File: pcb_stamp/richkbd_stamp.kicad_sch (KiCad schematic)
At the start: 52 parts, among them J1 USB_C_Receptacle_USB2.0, J2 OLED, K0 key-diode-led, K1 key-diode-led, K10 key-diode-led, K100 key-diode-led, K101 key-diode-led, K102 key-diode-led, K11 key-diode-led, K110 key-diode-led, K111 key-diode-led, K112 key-diode-led, K12 key-diode-led, K2 key-diode-led, K20 key-diode-led, K21 key-diode-led, K22 key-diode-led, K30 key-diode-led, K31 key-diode-led, K32 key-diode-led, K33 key-diode-led, K40 key-diode-led, K41 key-diode-led, K42 key-diode-led, K43 key-diode-led, K50 key-diode-led, K51 key-diode-led, K52 key-diode-led, K53 key-diode-led, K60 key-diode-led, K61 key-diode-led, K62 key-diode-led, K63 key-diode-led, K70 key-diode-led, K71 key-diode-led, K72 key-diode-led, K73 key-diode-led, K80 key-diode-led, K81 key-diode-led, K82 key-diode-led, K83 key-diode-led, K90 key-diode-led, K91 key-diode-led, K92 key-diode-led, U1 RP2040_Stamp

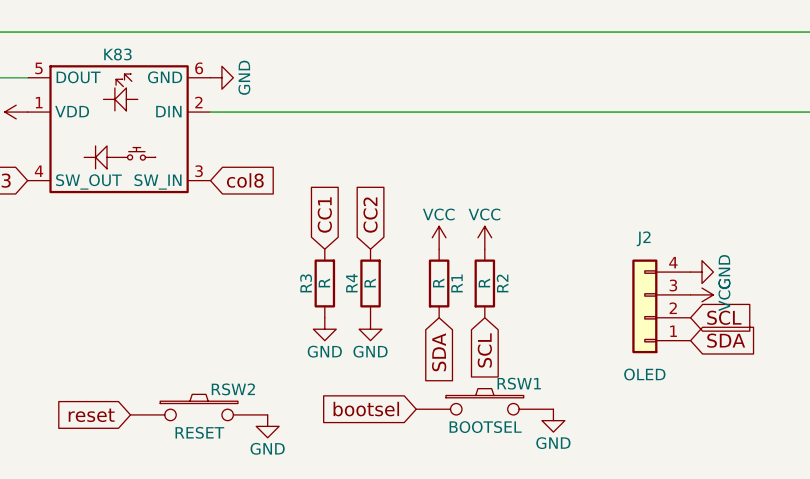
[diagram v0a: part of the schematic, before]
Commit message: Updated resistor values and moved lightsabres
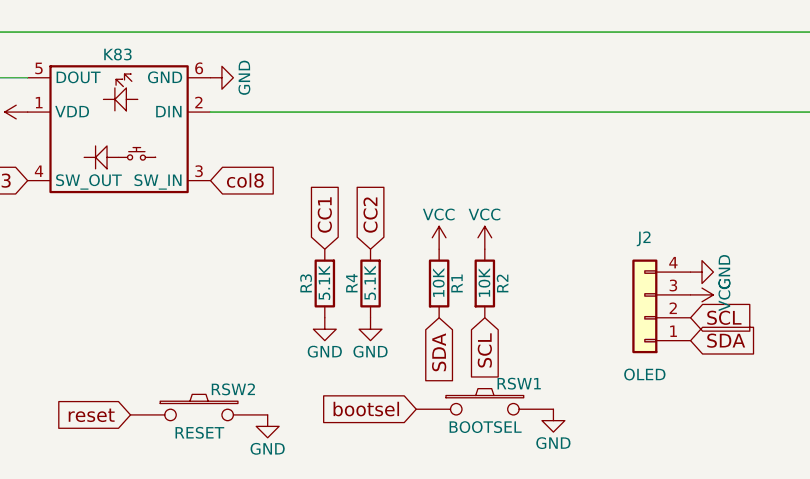
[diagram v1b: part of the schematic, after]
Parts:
- R1, R2: value R -> 10K
- R3, R4: value R -> 5.1K
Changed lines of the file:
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@@
     (in_bom yes) (on_board yes)
     (property "Reference" "R1" (id 0) (at 140.462 177.8 90))
-    (property "Value" "R" (id 1) (at 138.43 177.8 90))
+    (property "Value" "10K" (id 1) (at 138.43 177.8 90))
     (property "Footprint" "Resistor_SMD:R_0805_2012Metric" (id 2) (at 136.652 177.8 90)
       (effects (font (size 1.27 1.27)) hide)
@@
     (in_bom yes) (on_board yes)
     (property "Reference" "R2" (id 0) (at 145.542 177.8 90))
-    (property "Value" "R" (id 1) (at 143.51 177.8 90))
+    (property "Value" "10K" (id 1) (at 143.51 177.8 90))
     (property "Footprint" "Resistor_SMD:R_0805_2012Metric" (id 2) (at 141.732 177.8 90)
       (effects (font (size 1.27 1.27)) hide)
@@
     (in_bom yes) (on_board yes)
     (property "Reference" "R4" (id 0) (at 128.778 177.8 90))
-    (property "Value" "R" (id 1) (at 130.81 177.8 90))
+    (property "Value" "5.1K" (id 1) (at 130.81 177.8 90))
     (property "Footprint" "Resistor_SMD:R_0805_2012Metric" (id 2) (at 132.588 177.8 90)
       (effects (font (size 1.27 1.27)) hide)
@@
     (in_bom yes) (on_board yes)
     (property "Reference" "R3" (id 0) (at 123.698 177.8 90))
-    (property "Value" "R" (id 1) (at 125.73 177.8 90))
+    (property "Value" "5.1K" (id 1) (at 125.73 177.8 90))
     (property "Footprint" "Resistor_SMD:R_0805_2012Metric" (id 2) (at 127.508 177.8 90)
       (effects (font (size 1.27 1.27)) hide)
@@
     )
     (path "/00000000-0000-0000-0000-00005aa6d1f3"
-      (reference "R1") (unit 1) (value "R") (footprint "Resistor_SMD:R_0805_2012Metric")
+      (reference "R1") (unit 1) (value "10K") (footprint "Resistor_SMD:R_0805_2012Metric")
     )
     (path "/00000000-0000-0000-0000-00005aa6d2a6"
-      (reference "R2") (unit 1) (value "R") (footprint "Resistor_SMD:R_0805_2012Metric")
+      (reference "R2") (unit 1) (value "10K") (footprint "Resistor_SMD:R_0805_2012Metric")
     )
     (path "/dc4b8a19-92e0-4c35-a940-e928d580ba5b"
-      (reference "R3") (unit 1) (value "R") (footprint "Resistor_SMD:R_0805_2012Metric")
+      (reference "R3") (unit 1) (value "5.1K") (footprint "Resistor_SMD:R_0805_2012Metric")
     )
     (path "/387971ed-abb9-4f95-a329-18b3cdb7e9ad"
-      (reference "R4") (unit 1) (value "R") (footprint "Resistor_SMD:R_0805_2012Metric")
+      (reference "R4") (unit 1) (value "5.1K") (footprint "Resistor_SMD:R_0805_2012Metric")
     )
     (path "/00000000-0000-0000-0000-00005a5eb9e2"
